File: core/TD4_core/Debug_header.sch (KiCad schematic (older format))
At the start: 1 part

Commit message: Fixed minor core PCB errors
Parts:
- J2: renamed from J?; footprint (none) -> Connector_PinHeader_2.54mm:PinHeader_1x04_P2.54mm_Horizontal
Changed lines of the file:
@@
 $Descr A4 11693 8268
 encoding utf-8
-Sheet 24 30
+Sheet 29 30
 Title ""
 Date ""
@@
 F2 "Q[0..3]" O R 5300 2900 50
 F3 "A[0..3]" I L 4550 2900 50
-F4 "EN" I L 4550 3000 50
+F4 "~EN" I L 4550 3000 50
 $EndSheet
 Entry Wire Line
@@
 P 6300 2500
 AR Path="/5C7339E6" Ref="J?"  Part="1"
-AR Path="/5C72E552/5C7339E6" Ref="J?"  Part="1"
-AR Path="/5C74C5C4/5C7339E6" Ref="J?"  Part="1"
+AR Path="/5C72E552/5C7339E6" Ref="J2"  Part="1"
+AR Path="/5C74C5C4/5C7339E6" Ref="J3"  Part="1"
 AR Path="/5C758048/5C7339E6" Ref="J?"  Part="1"
-AR Path="/5C77FFF0/5C780016/5C7339E6" Ref="J?"  Part="1"
-F 0 "J?" H 6380 2492 50  0000 L CNN
+AR Path="/5C77FFF0/5C780016/5C7339E6" Ref="J4"  Part="1"
+F 0 "J2" H 6380 2492 50  0000 L CNN
 F 1 "Conn_01x04" H 6380 2401 50  0000 L CNN
-F 2 "" H 6300 2500 50  0001 C CNN
+F 2 "Connector_PinHeader_2.54mm:PinHeader_1x04_P2.54mm_Horizontal" H 6300 2500 50  0001 C CNN
 F 3 "~" H 6300 2500 50  0001 C CNN
 	1    6300 2500
@@
 Wire Wire Line
 	4200 3000 4550 3000
-Wire Bus Line
-	5800 2300 5800 2900
 Text HLabel 4200 2900 0    50   Input ~ 0
 In[0..3]
@@
 Text Label 4250 2900 0    50   ~ 0
 In[0..3]
+Wire Bus Line
+	5800 2300 5800 2900
 $EndSCHEMATC

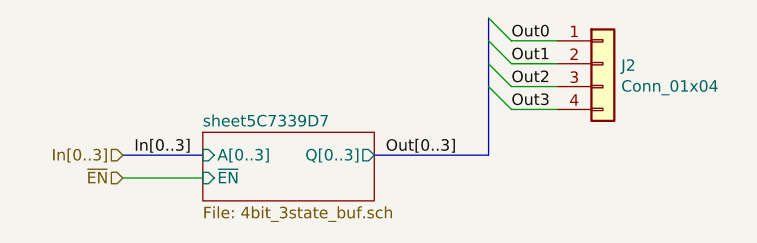
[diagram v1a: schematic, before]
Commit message: Added IN bus pull-ups in core
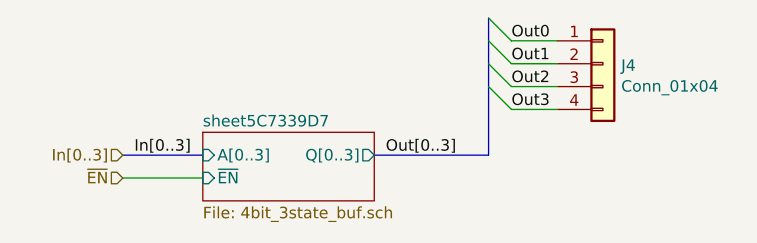
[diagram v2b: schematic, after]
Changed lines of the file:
@@
 AR Path="/5C758048/5C7339E6" Ref="J?"  Part="1"
 AR Path="/5C77FFF0/5C780016/5C7339E6" Ref="J4"  Part="1"
-F 0 "J2" H 6380 2492 50  0000 L CNN
+F 0 "J4" H 6380 2492 50  0000 L CNN
 F 1 "Conn_01x04" H 6380 2401 50  0000 L CNN
 F 2 "Connector_PinHeader_2.54mm:PinHeader_1x04_P2.54mm_Horizontal" H 6300 2500 50  0001 C CNN

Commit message: Replaced debug headers with vertical ones
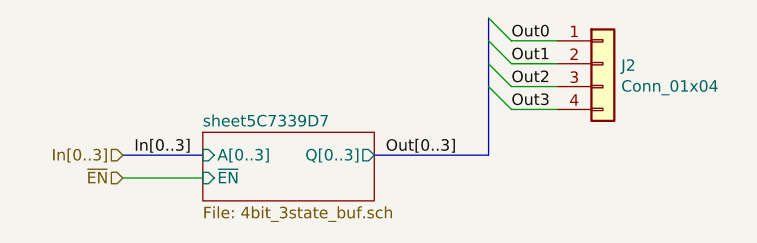
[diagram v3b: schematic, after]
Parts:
- J2: footprint Connector_PinHeader_2.54mm:PinHeader_1x04_P2.54mm_Horizontal -> Connector_PinHeader_2.54mm:PinHeader_1x04_P2.54mm_Vertical
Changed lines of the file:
@@
 $Descr A4 11693 8268
 encoding utf-8
-Sheet 29 30
+Sheet 24 30
 Title ""
 Date ""
@@
 AR Path="/5C758048/5C7339E6" Ref="J?"  Part="1"
 AR Path="/5C77FFF0/5C780016/5C7339E6" Ref="J4"  Part="1"
-F 0 "J4" H 6380 2492 50  0000 L CNN
+F 0 "J2" H 6380 2492 50  0000 L CNN
 F 1 "Conn_01x04" H 6380 2401 50  0000 L CNN
-F 2 "Connector_PinHeader_2.54mm:PinHeader_1x04_P2.54mm_Horizontal" H 6300 2500 50  0001 C CNN
+F 2 "Connector_PinHeader_2.54mm:PinHeader_1x04_P2.54mm_Vertical" H 6300 2500 50  0001 C CNN
 F 3 "~" H 6300 2500 50  0001 C CNN
 	1    6300 2500
